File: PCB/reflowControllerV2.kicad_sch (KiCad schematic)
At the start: 96 parts, among them J10 NEXTION_OB, J11 PWR, J12 A-1JB, J2 SSR2, J3 SSR1, J4 FAN1, J5 FAN2, J6 T1, J7 T2, J8 SWD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

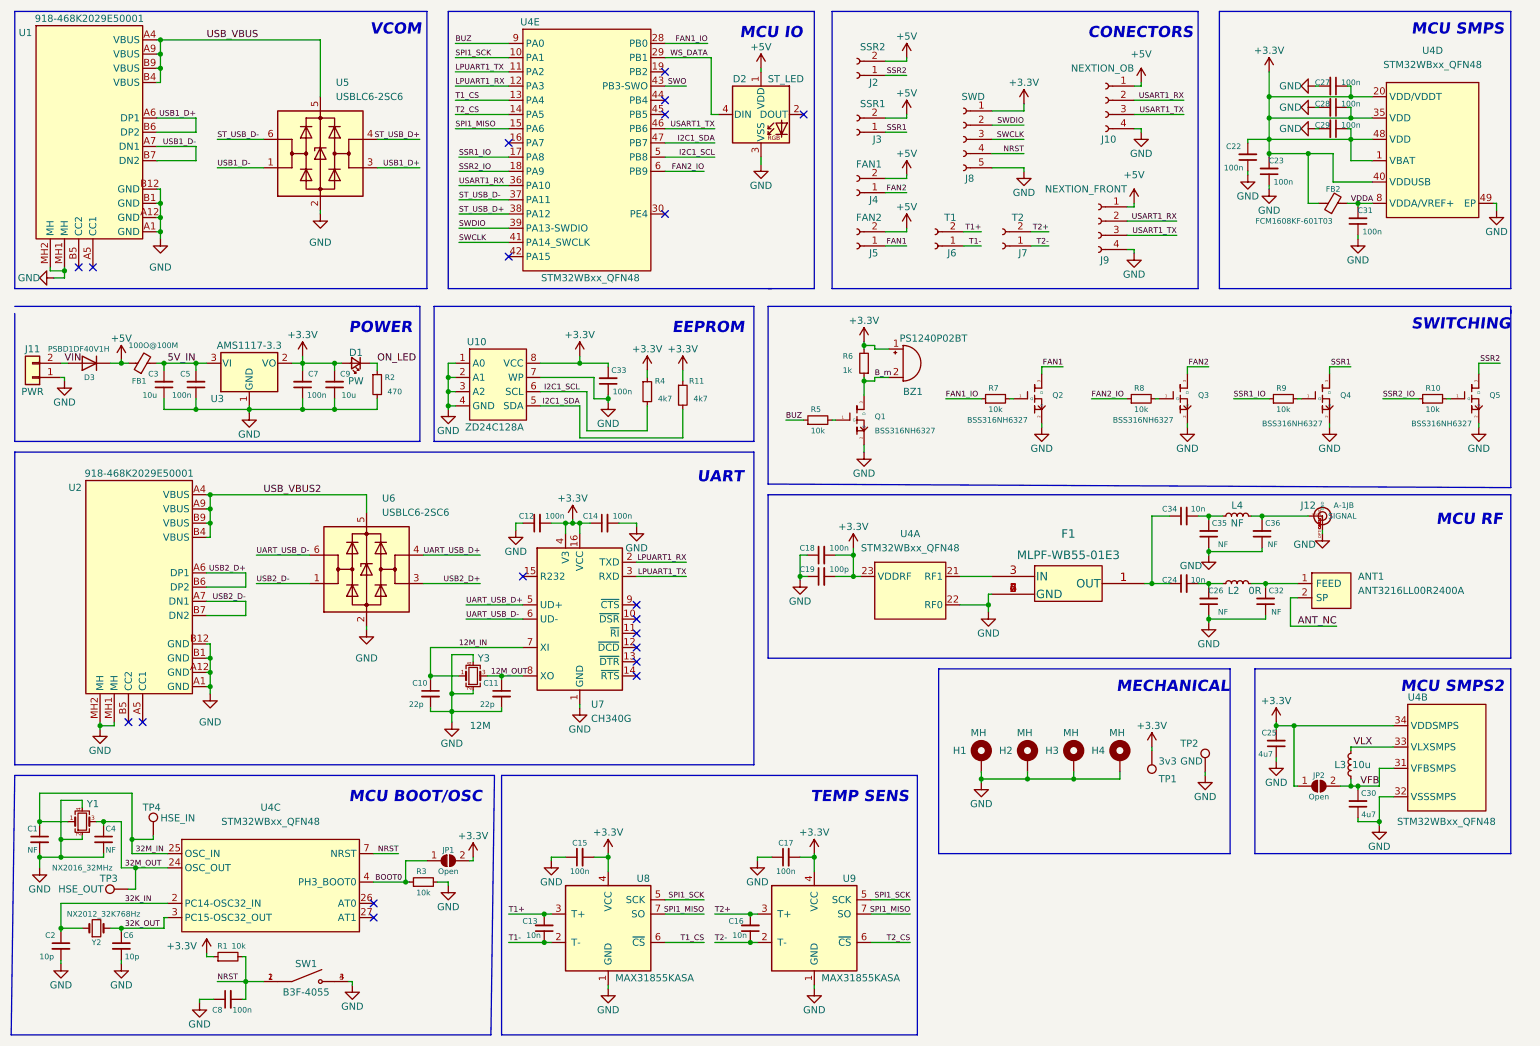
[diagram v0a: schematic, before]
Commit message: Reorganized schematic
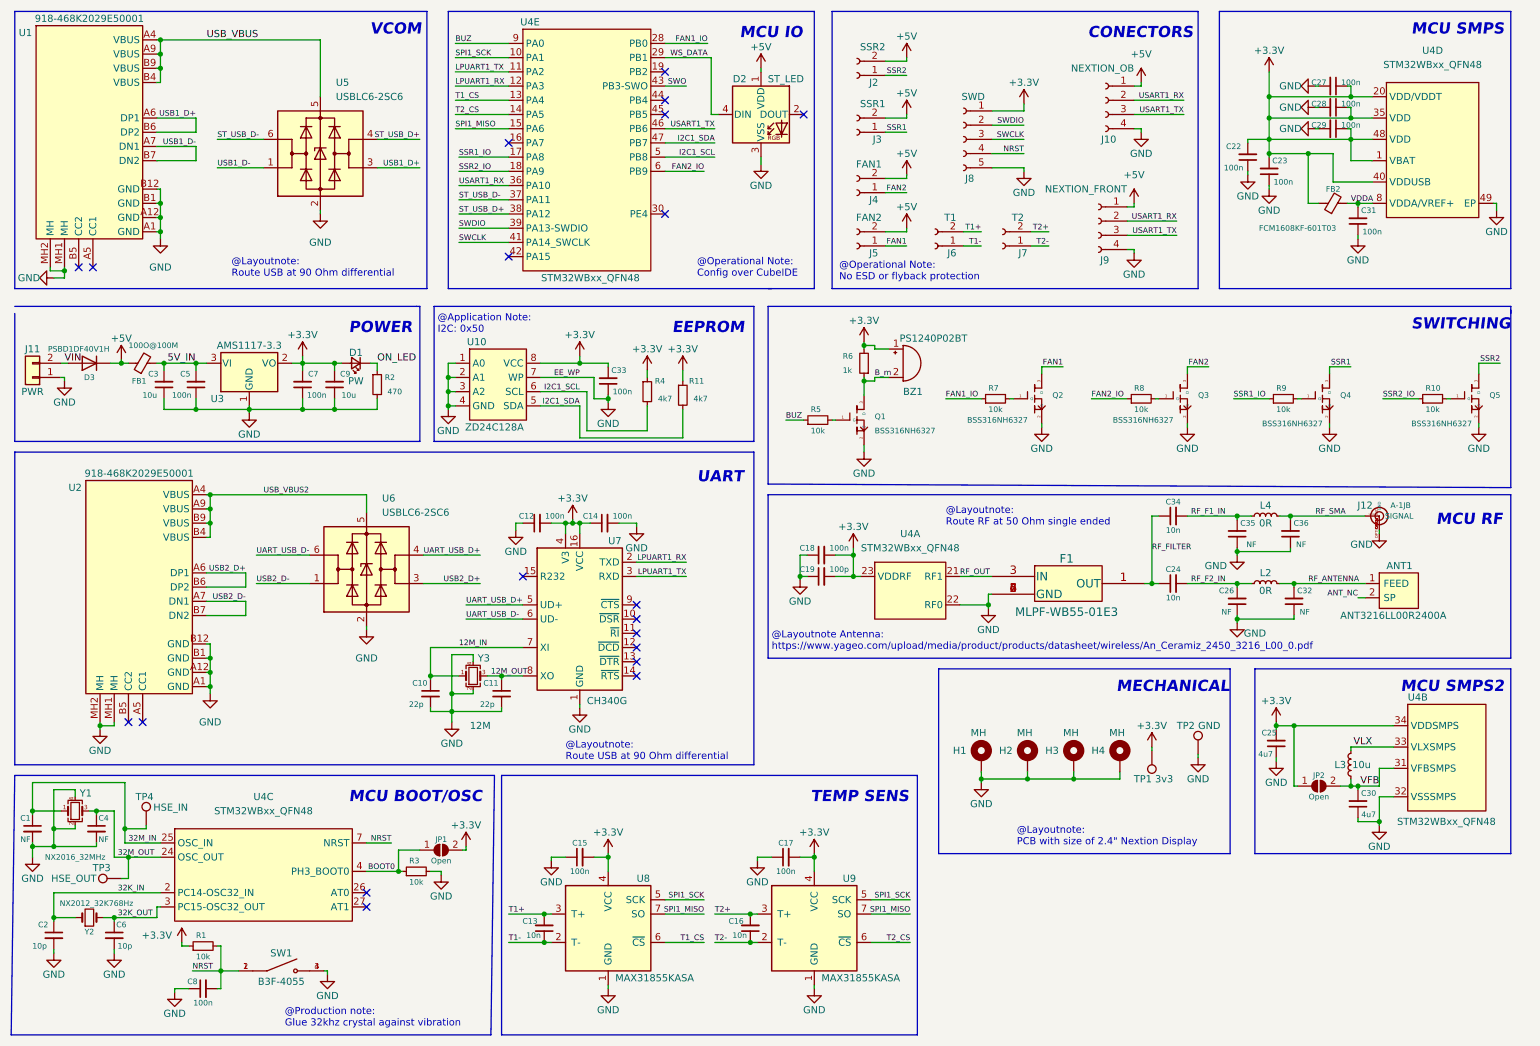
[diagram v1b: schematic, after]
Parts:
- L4: value NF -> 0R
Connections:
- net RF_ANTENNA: now reaches ANT1.1 (FEED), C32.2, L2.2
- net RF_F2_IN: now reaches C24.2, C26.2, L2.1
- net RF_FILTER: now reaches C24.1, C34.1, F1.1 (OUT)
- net RF_OUT: now reaches F1.3 (IN), U4.21 (RF1)
- net RF_F1_IN: now reaches C34.2, C35.2, L4.1
- net RF_SMA: now reaches C36.2, J12.SIGNAL, L4.2
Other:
- note added: "@Application Note: I2C: 0x50"
- note added: "@Layoutnote Antenna: https://www.yageo.com/upload/media/product/products/datasheet/wireless/An_Ceramiz_2450_3216_L00_0.pdf"
- note added: "@Layoutnote: PCB with size of 2.4" Nextion Display"
- note added: "@Layoutnote: Route RF at 50 Ohm single ended"
- note added: "@Layoutnote: Route USB at 90 Ohm differential"
- note added: "@Operational Note: Config over CubeIDE"
- note added: "@Operational Note: No ESD or flyback protection"
- note added: "@Production note: Glue 32khz crystal against vibration"
- moved on the sheet: ANT1, C1, C2, C24, C26, C32, C34, C35, C36, C4, C6, C8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
